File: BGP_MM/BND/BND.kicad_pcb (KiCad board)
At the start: 2 copper layers, 27 x 28 mm, 5 parts, among them J1 Conn_01x02, J2 Conn_01x03, P1 CONN_01X04, P2 Conn_01x02

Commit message: MM Routing complete
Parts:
- J1, J2: moved to F.Cu
- moved J2 5.08 mm to (106.1, 85.5), turned to 270 degrees
- moved J1 2.54 mm to (106.1, 93.8), turned to 270 degrees
- moved P1 0.20 mm to (127.9, 89.3)
- moved P2 0.20 mm to (127.9, 95.5)
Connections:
- J1 pad 1: VCC -> Net-(J1-Pad1)
- J1 pad 2: Net-(J1-Pad2) -> VCC
- J2 pad 1: Net-(J1-Pad2) -> Earth
- J2 pad 3: Earth -> Net-(J1-Pad1)
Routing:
- net Net-(J1-Pad2): track 3.22 -> 0.00 mm
- net Net-(J1-Pad1): track 0.00 -> 3.22 mm
- net /OUT: track 26.3 -> 28.7 mm
- added copper zone on F.Cu, net Earth
- added copper zone on B.Cu, net VCC
- removed copper zone on B.Cu, net Earth
- removed copper zone on F.Cu, net VCC

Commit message: MM Tweaks
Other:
- board text added: "MM Sabre Volume A/P CBD Design"
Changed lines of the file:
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@@
     (area 100.73412 69.174999 131.635 98.553333)
     (thickness 1.6)
-    (drawings 8)
+    (drawings 9)
     (tracks 31)
     (zones 0)
@@
     )
   )
+  (gr_text "MM Sabre\nVolume A/P\nCBD Design" (at 123 95) (layer F.SilkS)
+    (effects (font (size 0.6 0.6) (thickness 0.15)))
+  )
   (gr_line (start 103.3 97.7) (end 103.3 70.3) (angle 90) (layer Margin) (width 0.2))

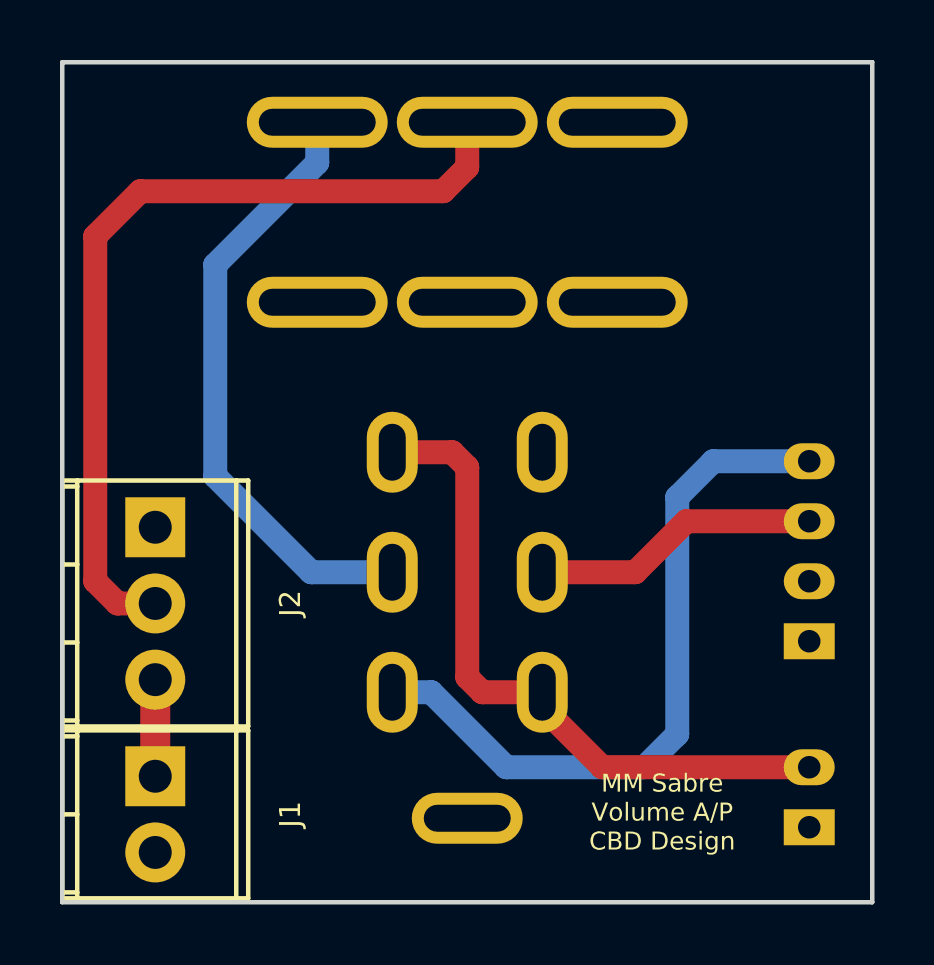
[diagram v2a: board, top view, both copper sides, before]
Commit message: MM Connector Verification
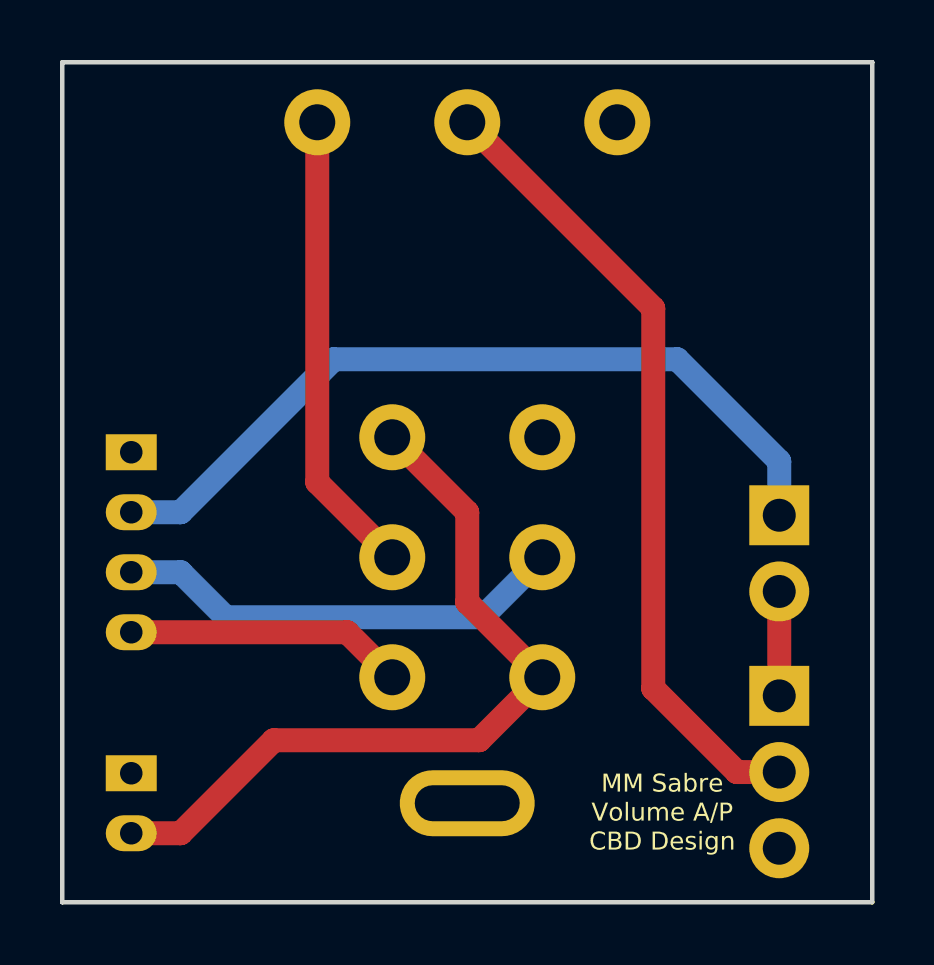
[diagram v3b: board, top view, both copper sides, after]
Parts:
- J1, J2: moved to B.Cu
- RV1: value Conn_01x13 -> CONN_01X10; footprint LIBS:Bournes_Blend_PP -> LIBS:Bournes_Blend_PP_PCB
- moved P1 23.5 mm to (105.3, 83.0), turned to 270 degrees
- moved P2 22.7 mm to (105.3, 93.7), turned to 270 degrees
- moved J1 22.5 mm to (126.9, 85.1)
- moved J2 21.5 mm to (126.9, 91.1)
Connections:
- J1 pad 1: Net-(J1-Pad1) -> VCC
- J1 pad 2: VCC -> Net-(J1-Pad2)
- J2 pad 1: Earth -> Net-(J1-Pad2)
- J2 pad 3: Net-(J1-Pad1) -> Earth
- P1 pad 3: /ACT_IN -> /ACT_O
- P1 pad 4: /ACT_OUT -> /ACT_I
- P2 pad 2: /PSV_OUT -> /PSV_I
- RV1 pad 1: /SEL -> /VOL_I
- RV1 pad 10: Net-(RV1-Pad10) -> Earth
- RV1 pad 4: Net-(RV1-Pad4) -> /PSV_I
- RV1 pad 5: Net-(RV1-Pad5) -> /VOL_I
- RV1 pad 6: Net-(RV1-Pad6) -> /ACT_I
- RV1 pad 7: /PSV_OUT -> Net-(RV1-Pad7)
- RV1 pad 8: /SEL -> /ACT_O
- RV1 pad 9: /ACT_OUT -> /PSV_I
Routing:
- net VCC: track 0.00 -> 26.9 mm
- net /PSV_I: track 0.00 -> 25.9 mm
- net /ACT_OUT: track 23.6 -> 0.00 mm
- net /PSV_OUT: track 22.4 -> 0.00 mm
- net /SEL: track 20.4 -> 0.00 mm
- net /VOL_I: track 0.00 -> 15.5 mm
- net /ACT_O: track 0.00 -> 15.1 mm
- net /ACT_IN: track 9.40 -> 0.00 mm
- net /ACT_I: track 0.00 -> 9.32 mm
- net Net-(J1-Pad2): track 0.00 -> 3.48 mm
- net Net-(J1-Pad1): track 3.22 -> 0.00 mm
- net /OUT: track 28.7 -> 26.8 mm
- added copper zone on B.Cu, net Earth
- removed copper zone on B.Cu, net VCC
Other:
- net class Default: trace_width 0.5 -> 0.8

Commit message: Board Labels
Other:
- board text added: "B+"
- board text added: "B-"
- board text added: "BASS"
- board text added: "JR"
- board text added: "JS"
- board text added: "JT"
- board text added: "TREBLE"
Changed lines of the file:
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@@
     (links 12)
     (no_connects 0)
-    (area 102.924999 69.924999 130.075001 98.075001)
+    (area 102.774999 69.174999 132.33588 98.475001)
     (thickness 1.6)
-    (drawings 9)
+    (drawings 16)
     (tracks 25)
     (zones 0)
@@
     (at 126.9 85.1 270)
     (descr "2-way 2.54mm pitch terminal block, Phoenix MPT series")
-    (fp_text reference J1 (at 1.27 4.50088 270) (layer B.SilkS)
+    (fp_text reference J1 (at -0.8 2.1 270) (layer B.SilkS)
       (effects (font (size 0.7 0.7) (thickness 0.15)) (justify mirror))
     )
@@
     (at 126.9 91.12 270)
     (descr "3-way 2.54mm pitch terminal block, Phoenix MPT series")
-    (fp_text reference J2 (at 2.54 4.50088 270) (layer B.SilkS)
+    (fp_text reference J2 (at -0.82 2.1 270) (layer B.SilkS)
       (effects (font (size 0.7 0.7) (thickness 0.15)) (justify mirror))
     )
@@
     (descr "JST PH series connector, B4B-PH-K, top entry type, through hole, Datasheet: http://www.jst-mfg.com/product/pdf/eng/ePH.pdf")
     (tags "connector jst ph")
-    (fp_text reference P1 (at 3 -3.8 270) (layer B.SilkS)
+    (fp_text reference P1 (at -0.6 -1.7 270) (layer B.SilkS)
       (effects (font (size 0.7 0.7) (thickness 0.15)) (justify mirror))
     )
@@
     (descr "JST PH series connector, B2B-PH-K, top entry type, through hole, Datasheet: http://www.jst-mfg.com/product/pdf/eng/ePH.pdf")
     (tags "connector jst ph")
-    (fp_text reference P2 (at 1.2 -2.8 270) (layer B.SilkS)
+    (fp_text reference P2 (at -0.7 -1.7 270) (layer B.SilkS)
       (effects (font (size 0.7 0.7) (thickness 0.15)) (justify mirror))
     )
@@
     )
   )
-  (gr_text "MM Sabre\nVolume A/P\nCBD Design" (at 123 95) (layer F.SilkS)
-    (effects (font (size 0.6 0.6) (thickness 0.15)))
-  )
+  (gr_text BASS (at 107 94.8 270) (layer F.SilkS)
+    (effects (font (size 0.6 0.6) (thickness 0.15)))
+  )
+  (gr_text TREBLE (at 106.9 86 270) (layer F.SilkS)
+    (effects (font (size 0.6 0.6) (thickness 0.15)))
+  )
+  (gr_text B+ (at 125 85.1 90) (layer F.SilkS)
+    (effects (font (size 0.6 0.6) (thickness 0.15)))
+  )
+  (gr_text B- (at 125 87.6 90) (layer F.SilkS)
+    (effects (font (size 0.6 0.6) (thickness 0.15)))
+  )
+  (gr_text JT (at 125 93.6 90) (layer F.SilkS)
+    (effects (font (size 0.6 0.6) (thickness 0.15)))
+  )
+  (gr_text JR (at 125 91.1 90) (layer F.SilkS)
+    (effects (font (size 0.6 0.6) (thickness 0.15)))
+  )
+  (gr_text JS (at 125 96.2 90) (layer F.SilkS)
+    (effects (font (size 0.6 0.6) (thickness 0.15)))
+  )
+  (gr_text "MM Sabre\nVolume A/P\nCBD Design" (at 126 75.8) (layer F.SilkS)
+    (effects (font (size 0.6 0.6) (thickness 0.15)))
+  )

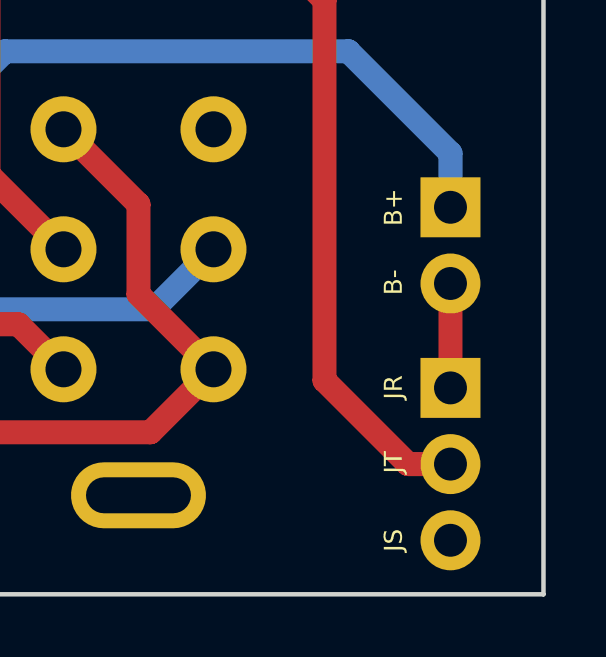
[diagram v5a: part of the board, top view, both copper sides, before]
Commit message: MM Gerbers Finished, Mid Stack Ammended J0
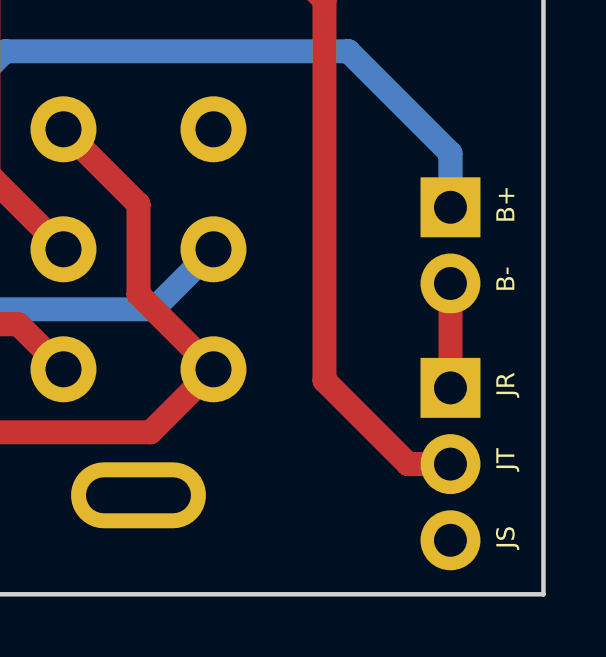
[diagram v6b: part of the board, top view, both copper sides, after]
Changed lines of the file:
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@@
-(kicad_pcb (version 4) (host pcbnew 4.0.4-1.fc24-product)
+(kicad_pcb (version 4) (host pcbnew 4.0.7)
   (general
     (links 12)
@@
     (effects (font (size 0.6 0.6) (thickness 0.15)))
   )
-  (gr_text B+ (at 125 85.1 90) (layer F.SilkS)
-    (effects (font (size 0.6 0.6) (thickness 0.15)))
-  )
-  (gr_text B- (at 125 87.6 90) (layer F.SilkS)
-    (effects (font (size 0.6 0.6) (thickness 0.15)))
-  )
-  (gr_text JT (at 125 93.6 90) (layer F.SilkS)
-    (effects (font (size 0.6 0.6) (thickness 0.15)))
-  )
-  (gr_text JR (at 125 91.1 90) (layer F.SilkS)
-    (effects (font (size 0.6 0.6) (thickness 0.15)))
-  )
-  (gr_text JS (at 125 96.2 90) (layer F.SilkS)
-    (effects (font (size 0.6 0.6) (thickness 0.15)))
-  )
+  (gr_text B+ (at 128.75 85 90) (layer F.SilkS)
+    (effects (font (size 0.6 0.6) (thickness 0.15)))
+  )
+  (gr_text B- (at 128.75 87.5 90) (layer F.SilkS)
+    (effects (font (size 0.6 0.6) (thickness 0.15)))
+  )
+  (gr_text JT (at 128.75 93.5 90) (layer F.SilkS)
+    (effects (font (size 0.6 0.6) (thickness 0.15)))
+  )
+  (gr_text JR (at 128.75 91 90) (layer F.SilkS)
+    (effects (font (size 0.6 0.6) (thickness 0.15)))
+  )
+  (gr_text JS (at 128.75 96.1 90) (layer F.SilkS)
+    (effects (font (size 0.6 0.6) (thickness 0.15)))
+  )

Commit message: MM Refactoring
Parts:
- removed P2: Conn_01x02, Connectors_JST:JST_PH_B2B-PH-K_02x2.00mm_Straight
- P1: value CONN_01X04 -> CONN_01X02; footprint Connectors_JST:JST_PH_B4B-PH-K_04x2.00mm_Straight -> Connectors_JST:JST_PH_B2B-PH-K_02x2.00mm_Straight
- RV1: value CONN_01X10 -> POT; footprint LIBS:Bournes_Blend_PP_PCB -> LIBS:Potentiometer_Alpha_RV16
- moved J2 19.2 mm to (109.7, 82.7), turned to 180 degrees
- moved P1 15.4 mm to (120.7, 83.5), turned to 90 degrees
- moved J1 11.7 mm to (115.4, 82.7), turned to 180 degrees
- moved RV1 2.50 mm to (113.0, 74.0)
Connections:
- P1 pad 2: VCC -> Net-(P1-Pad2)
- RV1 pad 1: /VOL_I -> Earth
- RV1 pad 3: Earth -> Net-(P1-Pad2)
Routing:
- net VCC: track 26.9 -> 0.00 mm
- net /PSV_I: track 25.9 -> 0.00 mm
- net /OUT: track 26.8 -> 11.1 mm
- net /VOL_I: track 15.5 -> 0.00 mm
- net /ACT_O: track 15.1 -> 0.00 mm
- net /ACT_I: track 9.32 -> 0.00 mm
- net Net-(P1-Pad2): track 0.00 -> 8.62 mm
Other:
- board size 27 x 28 mm -> 20 x 16 mm
- board text removed: "BASS"
- board text removed: "MM Sabre Volume A/P CBD Design"
- board text removed: "TREBLE"

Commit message: MM Refactoring
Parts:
- removed J2: Conn_01x03, Terminal_Blocks:TerminalBlock_Pheonix_MPT-2.54mm_3pol
- removed P1: CONN_01X02, Connectors_JST:JST_PH_B2B-PH-K_02x2.00mm_Straight
- J1: value Conn_01x02 -> Conn_01x03_Male; footprint Terminal_Blocks:TerminalBlock_Pheonix_MPT-2.54mm_2pol -> Pin_Headers:Pin_Header_Straight_1x03_Pitch2.54mm
- moved J1 1.65 mm to (115.0, 81.1), turned to 90 degrees
- moved RV1 0.50 mm to (112.5, 74.0)
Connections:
- J1 pad 1: VCC -> /IN
- J1 pad 2: Net-(J1-Pad2) -> /OUT
- RV1 pad 3: Net-(P1-Pad2) -> /IN
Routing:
- net Net-(P1-Pad2): track 8.62 -> 0.00 mm
- net /IN: track 0.00 -> 8.02 mm
- net /OUT: track 11.1 -> 7.00 mm
- net Net-(J1-Pad2): track 3.20 -> 0.00 mm
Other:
- board size 20 x 16 mm -> 17 x 13 mm
- board text removed: "B+"
- board text removed: "B-"
- board text removed: "JR"
- board text removed: "JS"
- board text removed: "JT"
